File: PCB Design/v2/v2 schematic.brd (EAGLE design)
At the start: 100 x 80 mm, 9 parts

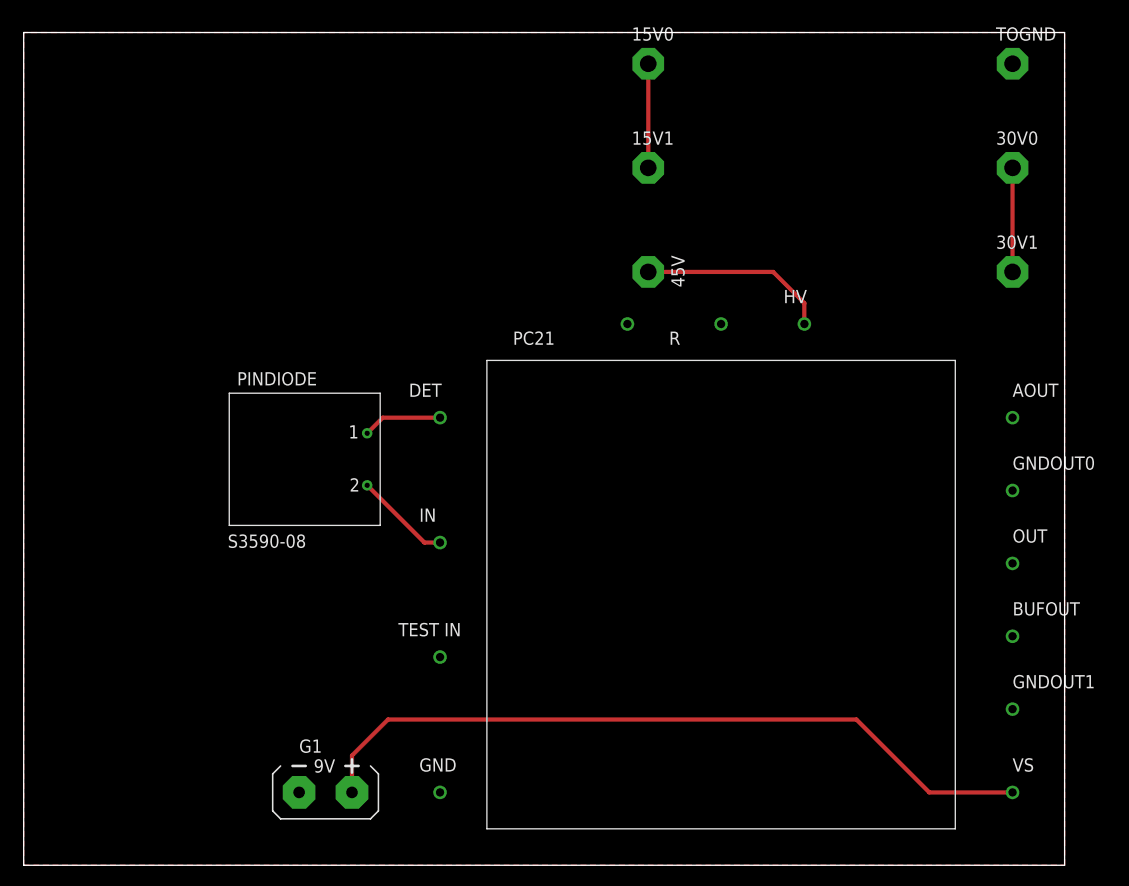
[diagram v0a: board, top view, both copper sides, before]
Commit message: Added SHARD-1 Library
Finalised v2 board for manufacturing.

Signed-off-by: joncrabb <jc00300@surrey.ac.uk>
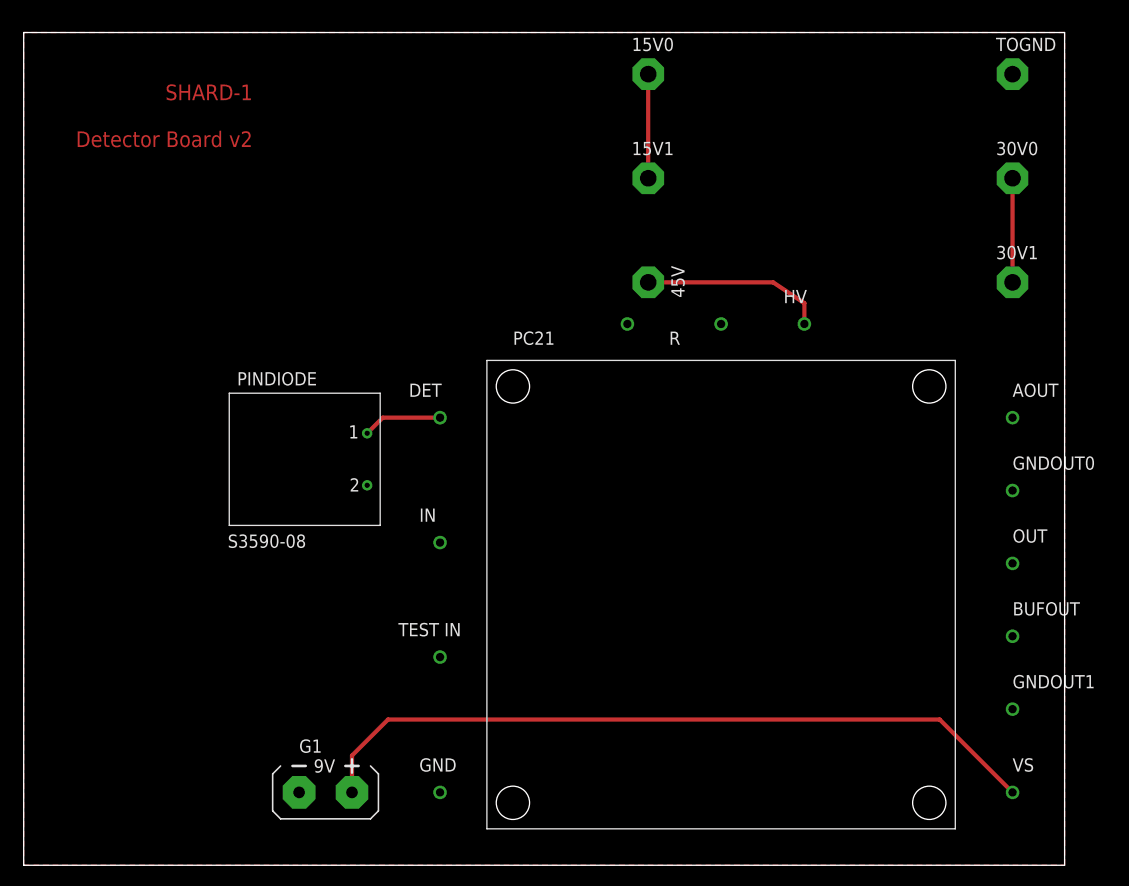
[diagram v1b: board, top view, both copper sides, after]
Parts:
- moved 15V0 1.00 mm to (60.0, 76.0)
- moved 15V1 1.00 mm to (60.0, 66.0)
- moved 30V0 1.00 mm to (95.0, 66.0)
- moved 30V1 1.00 mm to (95.0, 56.0)
- moved 45V 1.00 mm to (60.0, 56.0)
- moved TOGND 1.00 mm to (95.0, 76.0)
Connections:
- removed net N$5: PC21.IN, PINDIODE.2
- net GND: now also PINDIODE.2
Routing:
- net N$5: track 9.28 -> 0.00 mm
- net N$1: track 18.2 -> 17.6 mm
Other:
- board text added: "SHARD-1 Detector Board v2"
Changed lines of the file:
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@@
 <wire x1="100" y1="80" x2="0" y2="80" width="0" layer="20"/>
 <wire x1="0" y1="80" x2="0" y2="0" width="0" layer="20"/>
+<text x="22" y="75" size="1.5" layer="1" rot="R180">SHARD-1
+Detector Board v2</text>
+<hole x="47" y="46" drill="3.2"/>
+<hole x="87" y="46" drill="3.2"/>
+<hole x="87" y="6" drill="3.2"/>
+<hole x="47" y="6" drill="3.2"/>
 </plain>
 <attributes>
@@
 </autorouter>
 <elements>
-<element name="PC21" library="SHARD" package="A111" value="A111" x="67" y="26"/>
-<element name="45V" library="keystone" package="TP-063" value="TP-063" x="60" y="57" rot="R270"/>
-<element name="30V1" library="keystone" package="TP-063" value="TP-063" x="95" y="57"/>
-<element name="30V0" library="keystone" package="TP-063" value="TP-063" x="95" y="67"/>
-<element name="15V0" library="keystone" package="TP-063" value="TP-063" x="60" y="77"/>
-<element name="15V1" library="keystone" package="TP-063" value="TP-063" x="60" y="67"/>
-<element name="TOGND" library="keystone" package="TP-063" value="TP-063" x="95" y="77"/>
+<element name="45V" library="keystone" package="TP-063" value="TP-063" x="60" y="56" rot="R270"/>
+<element name="30V1" library="keystone" package="TP-063" value="TP-063" x="95" y="56"/>
+<element name="30V0" library="keystone" package="TP-063" value="TP-063" x="95" y="66"/>
+<element name="15V0" library="keystone" package="TP-063" value="TP-063" x="60" y="76"/>
+<element name="15V1" library="keystone" package="TP-063" value="TP-063" x="60" y="66"/>
+<element name="TOGND" library="keystone" package="TP-063" value="TP-063" x="95" y="76"/>
 <element name="G1" library="battery" package="AB9V" value="AB9V" x="29" y="7" rot="R270"/>
 <element name="PINDIODE" library="SHARD" package="S3590-08" value="S3590-08" x="27" y="39"/>
+<element name="PC21" library="SHARD" package="A111" value="A111" x="67" y="26"/>
 </elements>
 <signals>
 <signal name="N$1">
+<contactref element="45V" pad="1"/>
+<wire x1="72" y1="56" x2="75" y2="54" width="0.4064" layer="1"/>
+<wire x1="72" y1="56" x2="60" y2="56" width="0.4064" layer="1"/>
 <contactref element="PC21" pad="HV"/>
-<contactref element="45V" pad="1"/>
-<wire x1="72" y1="57" x2="75" y2="54" width="0.4064" layer="1"/>
 <wire x1="75" y1="54" x2="75" y2="52" width="0.4064" layer="1"/>
-<wire x1="72" y1="57" x2="60" y2="57" width="0.4064" layer="1"/>
 </signal>
 <signal name="N$2">
 <contactref element="30V1" pad="1"/>
 <contactref element="30V0" pad="1"/>
-<wire x1="95" y1="67" x2="95" y2="57" width="0.4064" layer="1"/>
+<wire x1="95" y1="66" x2="95" y2="56" width="0.4064" layer="1"/>
 </signal>
 <signal name="N$3">
 <contactref element="15V1" pad="1"/>
 <contactref element="15V0" pad="1"/>
-<wire x1="60" y1="77" x2="60" y2="67" width="0.4064" layer="1"/>
+<wire x1="60" y1="76" x2="60" y2="66" width="0.4064" layer="1"/>
 </signal>
 <signal name="GND">
 <contactref element="TOGND" pad="1"/>
-<contactref element="PC21" pad="GND"/>
-<contactref element="PC21" pad="GNDOUT1"/>
 <contactref element="G1" pad="-"/>
-<contactref element="PC21" pad="GNDOUT0"/>
 <polygon width="0.4064" layer="1" isolate="0.5">
 <vertex x="0" y="0"/>
@@
 <vertex x="0" y="78"/>
 </polygon>
+<contactref element="PC21" pad="GND"/>
+<contactref element="PC21" pad="GNDOUT1"/>
+<contactref element="PC21" pad="GNDOUT0"/>
+<contactref element="PINDIODE" pad="2"/>
 </signal>
 <signal name="N$4">
-<contactref element="PC21" pad="VS"/>
 <contactref element="G1" pad="+"/>
 <wire x1="31.54" y1="7" x2="31.54" y2="10.54" width="0.4064" layer="1"/>
 <wire x1="31.54" y1="10.54" x2="35" y2="14" width="0.4064" layer="1"/>
-<wire x1="35" y1="14" x2="80" y2="14" width="0.4064" layer="1"/>
-<wire x1="80" y1="14" x2="87" y2="7" width="0.4064" layer="1"/>
-<wire x1="87" y1="7" x2="95" y2="7" width="0.4064" layer="1"/>
-</signal>
-<signal name="N$5">
-<contactref element="PINDIODE" pad="2"/>
-<contactref element="PC21" pad="IN"/>
-<wire x1="33" y1="36.5" x2="38.5" y2="31" width="0.4064" layer="1"/>
-<wire x1="38.5" y1="31" x2="40" y2="31" width="0.4064" layer="1"/>
+<wire x1="35" y1="14" x2="88" y2="14" width="0.4064" layer="1"/>
+<contactref element="PC21" pad="VS"/>
+<wire x1="88" y1="14" x2="95" y2="7" width="0.4064" layer="1"/>
 </signal>
 <signal name="N$6">
 <contactref element="PINDIODE" pad="1"/>
+<wire x1="33" y1="41.5" x2="34.5" y2="43" width="0.4064" layer="1"/>
 <contactref element="PC21" pad="DET"/>
-<wire x1="33" y1="41.5" x2="34.5" y2="43" width="0.4064" layer="1"/>
 <wire x1="34.5" y1="43" x2="40" y2="43" width="0.4064" layer="1"/>
 </signal>
@@
 </board>
 </drawing>
+<compatibility>
+<note version="6.3" minversion="6.2.2" severity="warning">
+Since Version 6.2.2 text objects can contain more than one line,
+which will not be processed correctly with this version.
+</note>
+</compatibility>
 </eagle>

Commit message: Updated PCB design so diode is now reversed bias (correct)
Signed-off-by: joncrabb <jc00300@surrey.ac.uk>
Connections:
- net GND: now also PINDIODE.1; no longer PINDIODE.2
- net N$6: now also PINDIODE.2; no longer PINDIODE.1
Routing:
- net N$6: track 7.62 -> 12.0 mm
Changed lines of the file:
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@@
 <contactref element="PC21" pad="GNDOUT1"/>
 <contactref element="PC21" pad="GNDOUT0"/>
-<contactref element="PINDIODE" pad="2"/>
+<contactref element="PINDIODE" pad="1"/>
 </signal>
 <signal name="N$4">
@@
 </signal>
 <signal name="N$6">
-<contactref element="PINDIODE" pad="1"/>
-<wire x1="33" y1="41.5" x2="34.5" y2="43" width="0.4064" layer="1"/>
 <contactref element="PC21" pad="DET"/>
-<wire x1="34.5" y1="43" x2="40" y2="43" width="0.4064" layer="1"/>
+<contactref element="PINDIODE" pad="2"/>
+<wire x1="33" y1="36.5" x2="37.5" y2="36.5" width="0.4064" layer="1"/>
+<wire x1="37.5" y1="36.5" x2="40" y2="39" width="0.4064" layer="1"/>
+<wire x1="40" y1="39" x2="40" y2="43" width="0.4064" layer="1"/>
 </signal>
 </signals>

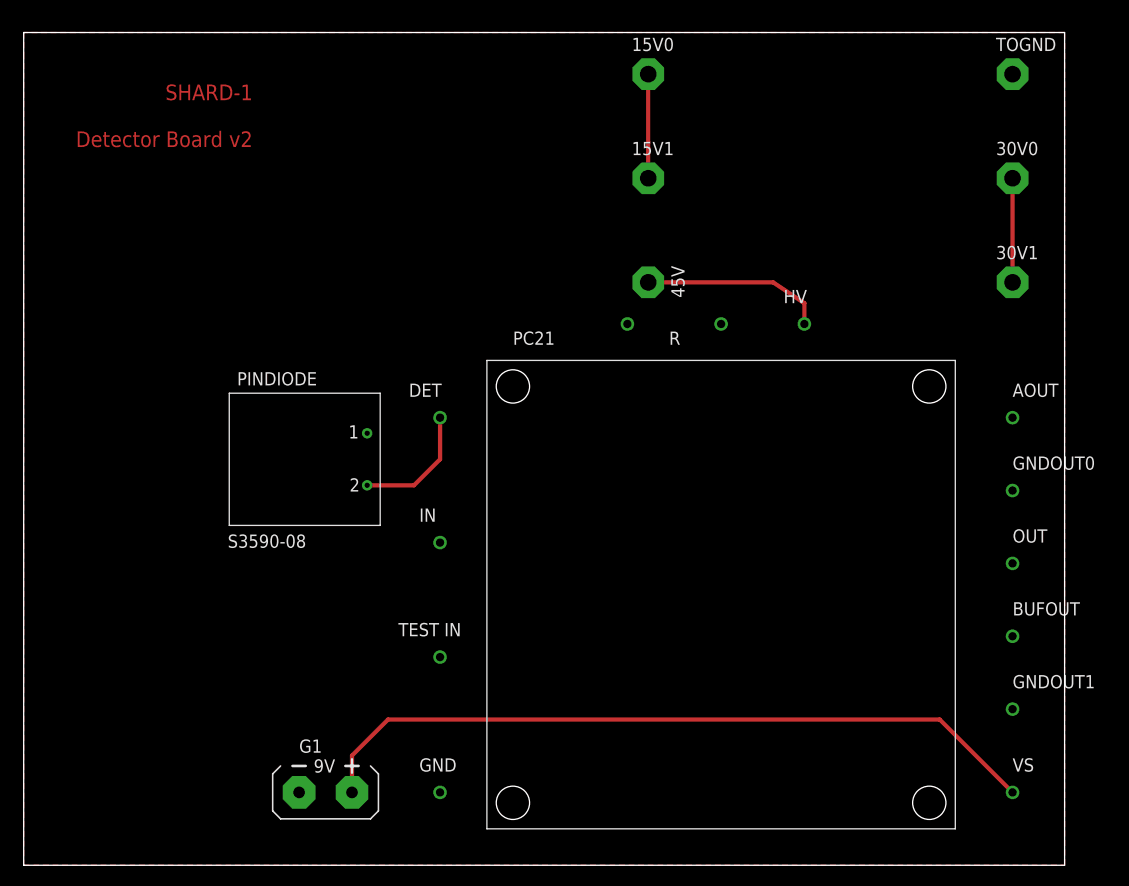
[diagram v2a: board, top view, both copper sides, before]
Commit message: Updated design so the batteries now fit.
Also discovered a problem with the battery clips having two holes!

Fixed design for it now (have to drill holes separately)

Signed-off-by: joncrabb <jc00300@surrey.ac.uk>
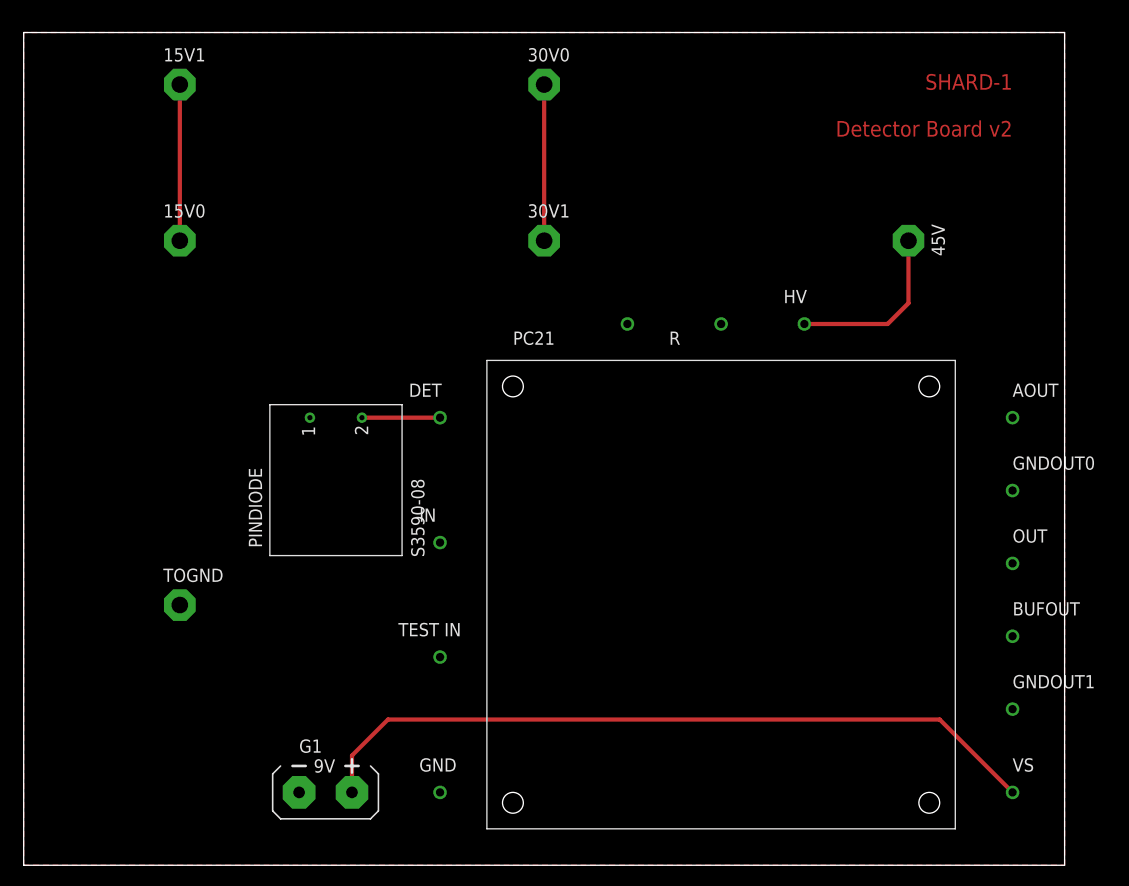
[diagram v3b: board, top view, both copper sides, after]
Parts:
- moved TOGND 94.9 mm to (15.0, 25.0)
- moved 15V0 47.8 mm to (15.0, 60.0)
- moved 15V1 45.9 mm to (15.0, 75.0)
- moved 30V0 45.9 mm to (50.0, 75.0)
- moved 30V1 45.2 mm to (50.0, 60.0)
- moved 45V 25.3 mm to (85.0, 60.0)
- moved PINDIODE 3.61 mm to (30.0, 37.0), turned to 90 degrees
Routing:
- net N$3: track 10.0 -> 15.0 mm
- net N$2: track 10.0 -> 15.0 mm
- net N$6: track 12.0 -> 7.50 mm
- net N$1: track 17.6 -> 16.8 mm
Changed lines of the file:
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@@
 <wire x1="100" y1="80" x2="0" y2="80" width="0" layer="20"/>
 <wire x1="0" y1="80" x2="0" y2="0" width="0" layer="20"/>
-<text x="22" y="75" size="1.5" layer="1" rot="R180">SHARD-1
+<text x="95" y="76" size="1.5" layer="1" rot="R180">SHARD-1
 Detector Board v2</text>
-<hole x="47" y="46" drill="3.2"/>
-<hole x="87" y="46" drill="3.2"/>
-<hole x="87" y="6" drill="3.2"/>
-<hole x="47" y="6" drill="3.2"/>
+<hole x="47" y="46" drill="2"/>
+<hole x="87" y="46" drill="2"/>
+<hole x="87" y="6" drill="2"/>
+<hole x="47" y="6" drill="2"/>
 </plain>
 <attributes>
@@
 </autorouter>
 <elements>
-<element name="45V" library="keystone" package="TP-063" value="TP-063" x="60" y="56" rot="R270"/>
-<element name="30V1" library="keystone" package="TP-063" value="TP-063" x="95" y="56"/>
-<element name="30V0" library="keystone" package="TP-063" value="TP-063" x="95" y="66"/>
-<element name="15V0" library="keystone" package="TP-063" value="TP-063" x="60" y="76"/>
-<element name="15V1" library="keystone" package="TP-063" value="TP-063" x="60" y="66"/>
-<element name="TOGND" library="keystone" package="TP-063" value="TP-063" x="95" y="76"/>
+<element name="45V" library="keystone" package="TP-063" value="TP-063" x="85" y="60" rot="R270"/>
+<element name="30V1" library="keystone" package="TP-063" value="TP-063" x="50" y="60"/>
+<element name="30V0" library="keystone" package="TP-063" value="TP-063" x="50" y="75"/>
+<element name="15V0" library="keystone" package="TP-063" value="TP-063" x="15" y="60"/>
+<element name="15V1" library="keystone" package="TP-063" value="TP-063" x="15" y="75"/>
+<element name="TOGND" library="keystone" package="TP-063" value="TP-063" x="15" y="25"/>
 <element name="G1" library="battery" package="AB9V" value="AB9V" x="29" y="7" rot="R270"/>
-<element name="PINDIODE" library="SHARD" package="S3590-08" value="S3590-08" x="27" y="39"/>
+<element name="PINDIODE" library="SHARD" package="S3590-08" value="S3590-08" x="30" y="37" rot="R90"/>
 <element name="PC21" library="SHARD" package="A111" value="A111" x="67" y="26"/>
 </elements>
@@
 <signal name="N$1">
 <contactref element="45V" pad="1"/>
-<wire x1="72" y1="56" x2="75" y2="54" width="0.4064" layer="1"/>
-<wire x1="72" y1="56" x2="60" y2="56" width="0.4064" layer="1"/>
 <contactref element="PC21" pad="HV"/>
-<wire x1="75" y1="54" x2="75" y2="52" width="0.4064" layer="1"/>
+<wire x1="75" y1="52" x2="83" y2="52" width="0.4064" layer="1"/>
+<wire x1="83" y1="52" x2="85" y2="54" width="0.4064" layer="1"/>
+<wire x1="85" y1="54" x2="85" y2="60" width="0.4064" layer="1"/>
 </signal>
 <signal name="N$2">
 <contactref element="30V1" pad="1"/>
 <contactref element="30V0" pad="1"/>
-<wire x1="95" y1="66" x2="95" y2="56" width="0.4064" layer="1"/>
+<wire x1="50" y1="60" x2="50" y2="75" width="0.4064" layer="1"/>
 </signal>
 <signal name="N$3">
 <contactref element="15V1" pad="1"/>
 <contactref element="15V0" pad="1"/>
-<wire x1="60" y1="76" x2="60" y2="66" width="0.4064" layer="1"/>
+<wire x1="15" y1="75" x2="15" y2="60" width="0.4064" layer="1"/>
 </signal>
 <signal name="GND">
@@
 <contactref element="PC21" pad="DET"/>
 <contactref element="PINDIODE" pad="2"/>
-<wire x1="33" y1="36.5" x2="37.5" y2="36.5" width="0.4064" layer="1"/>
-<wire x1="37.5" y1="36.5" x2="40" y2="39" width="0.4064" layer="1"/>
-<wire x1="40" y1="39" x2="40" y2="43" width="0.4064" layer="1"/>
+<wire x1="32.5" y1="43" x2="40" y2="43" width="0.4064" layer="1"/>
 </signal>
 </signals>

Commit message: Final v2 design
Signed-off-by: joncrabb <jc00300@surrey.ac.uk>
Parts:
- moved 15V0 5.10 mm to (10.0, 59.0)
- moved 15V1 5.10 mm to (10.0, 74.0)
- moved 30V0 5.00 mm to (45.0, 75.0)
- moved 30V1 5.00 mm to (45.0, 60.0)
- moved 45V 5.00 mm to (80.0, 60.0)
- moved TOGND 5.00 mm to (10.0, 25.0)
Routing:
- net N$1: track 16.8 -> 11.2 mm
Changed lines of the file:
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@@
 </autorouter>
 <elements>
-<element name="45V" library="keystone" package="TP-063" value="TP-063" x="85" y="60" rot="R270"/>
-<element name="30V1" library="keystone" package="TP-063" value="TP-063" x="50" y="60"/>
-<element name="30V0" library="keystone" package="TP-063" value="TP-063" x="50" y="75"/>
-<element name="15V0" library="keystone" package="TP-063" value="TP-063" x="15" y="60"/>
-<element name="15V1" library="keystone" package="TP-063" value="TP-063" x="15" y="75"/>
-<element name="TOGND" library="keystone" package="TP-063" value="TP-063" x="15" y="25"/>
+<element name="45V" library="keystone" package="TP-063" value="TP-063" x="80" y="60" rot="R270"/>
+<element name="30V1" library="keystone" package="TP-063" value="TP-063" x="45" y="60"/>
+<element name="30V0" library="keystone" package="TP-063" value="TP-063" x="45" y="75"/>
+<element name="15V0" library="keystone" package="TP-063" value="TP-063" x="10" y="59"/>
+<element name="15V1" library="keystone" package="TP-063" value="TP-063" x="10" y="74"/>
+<element name="TOGND" library="keystone" package="TP-063" value="TP-063" x="10" y="25"/>
 <element name="G1" library="battery" package="AB9V" value="AB9V" x="29" y="7" rot="R270"/>
 <element name="PINDIODE" library="SHARD" package="S3590-08" value="S3590-08" x="30" y="37" rot="R90"/>
@@
 <contactref element="45V" pad="1"/>
 <contactref element="PC21" pad="HV"/>
-<wire x1="75" y1="52" x2="83" y2="52" width="0.4064" layer="1"/>
-<wire x1="83" y1="52" x2="85" y2="54" width="0.4064" layer="1"/>
-<wire x1="85" y1="54" x2="85" y2="60" width="0.4064" layer="1"/>
+<wire x1="75" y1="52" x2="77" y2="52" width="0.4064" layer="1"/>
+<wire x1="77" y1="52" x2="80" y2="55" width="0.4064" layer="1"/>
+<wire x1="80" y1="55" x2="80" y2="60" width="0.4064" layer="1"/>
 </signal>
 <signal name="N$2">
 <contactref element="30V1" pad="1"/>
 <contactref element="30V0" pad="1"/>
-<wire x1="50" y1="60" x2="50" y2="75" width="0.4064" layer="1"/>
+<wire x1="45" y1="60" x2="45" y2="75" width="0.4064" layer="1"/>
 </signal>
 <signal name="N$3">
 <contactref element="15V1" pad="1"/>
 <contactref element="15V0" pad="1"/>
-<wire x1="15" y1="75" x2="15" y2="60" width="0.4064" layer="1"/>
+<wire x1="10" y1="74" x2="10" y2="59" width="0.4064" layer="1"/>
 </signal>
 <signal name="GND">
